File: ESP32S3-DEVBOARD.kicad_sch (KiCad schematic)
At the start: 61 parts, among them J1 PinHeader_1x22_P2.54mm_Vertic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, J2 PinHeader_1x22_P2.54mm_Vertic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, J3 G-Switch_GT-USB-7010ASV, J4 G-Switch_GT-USB-7010ASV, Q1 BC817-40,215, Q2 BC817-40,215, SW1 TS-1088-AR02016, SW2 TS-1088-AR02016, SW3 TS-1088-AR02016, SW4 TS-1088-AR02016, U1 AMS1117-3.3, U2 ESP32-S3-WROOM-1, U3 USBLC6-2P6, U4 CP2102N-A02-GQFN28R, U5 BMI270, U6 USBLC6-2P6

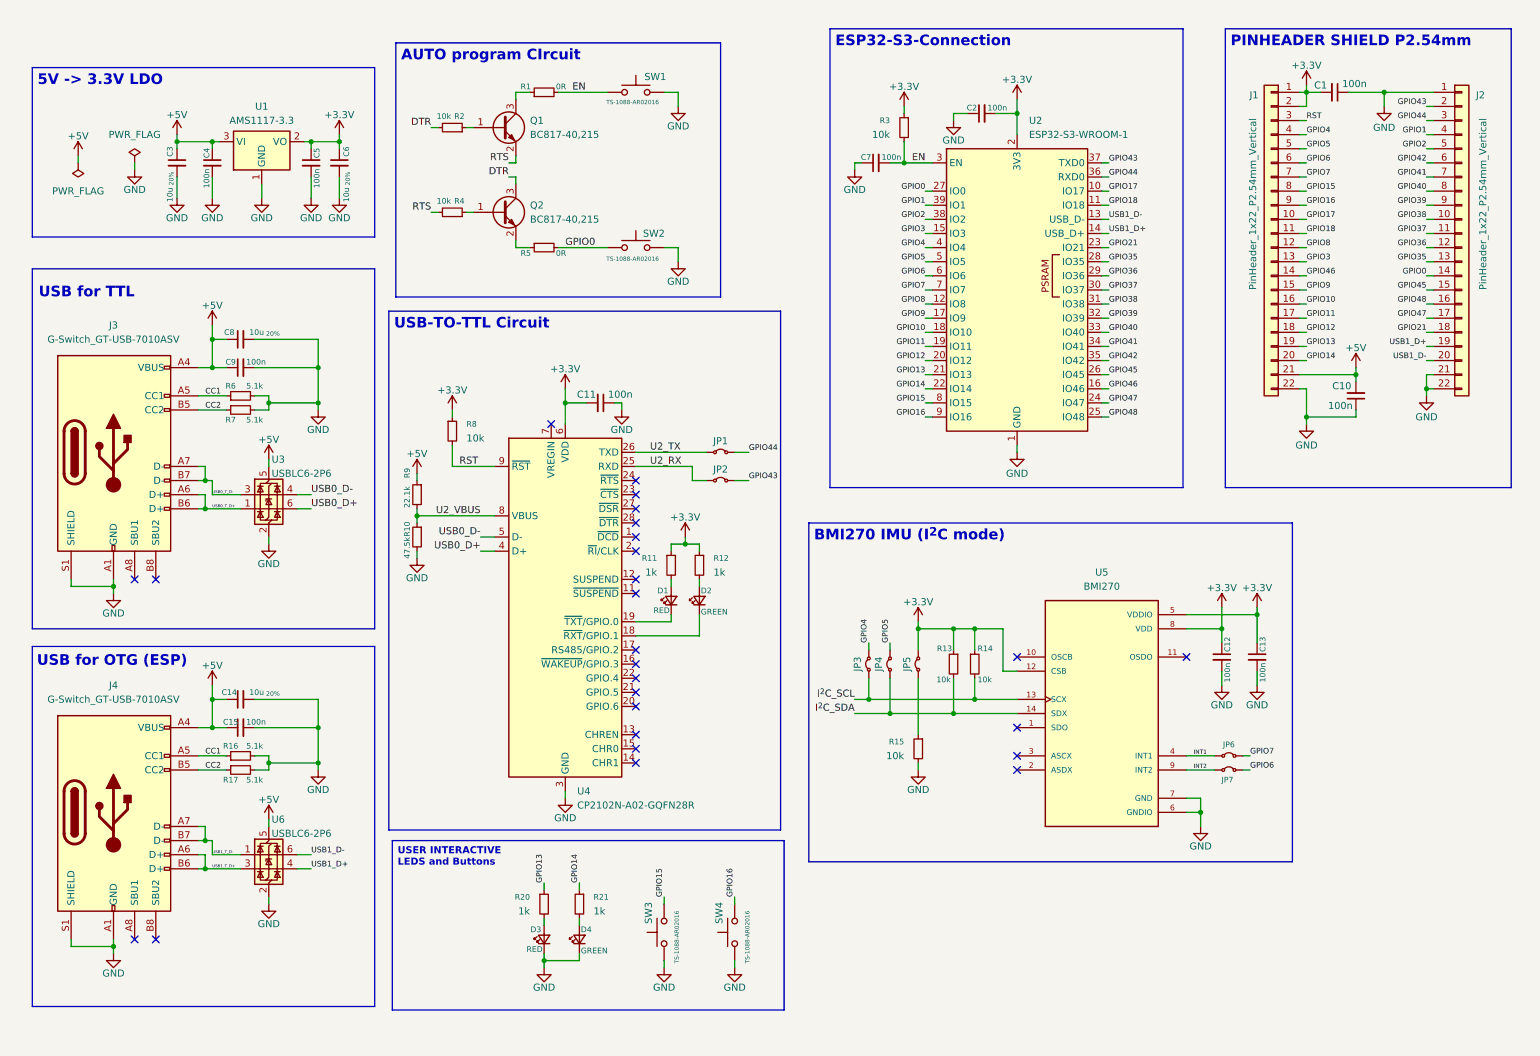
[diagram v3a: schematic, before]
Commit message: Removed jumpers, and added dipswitch to schematics
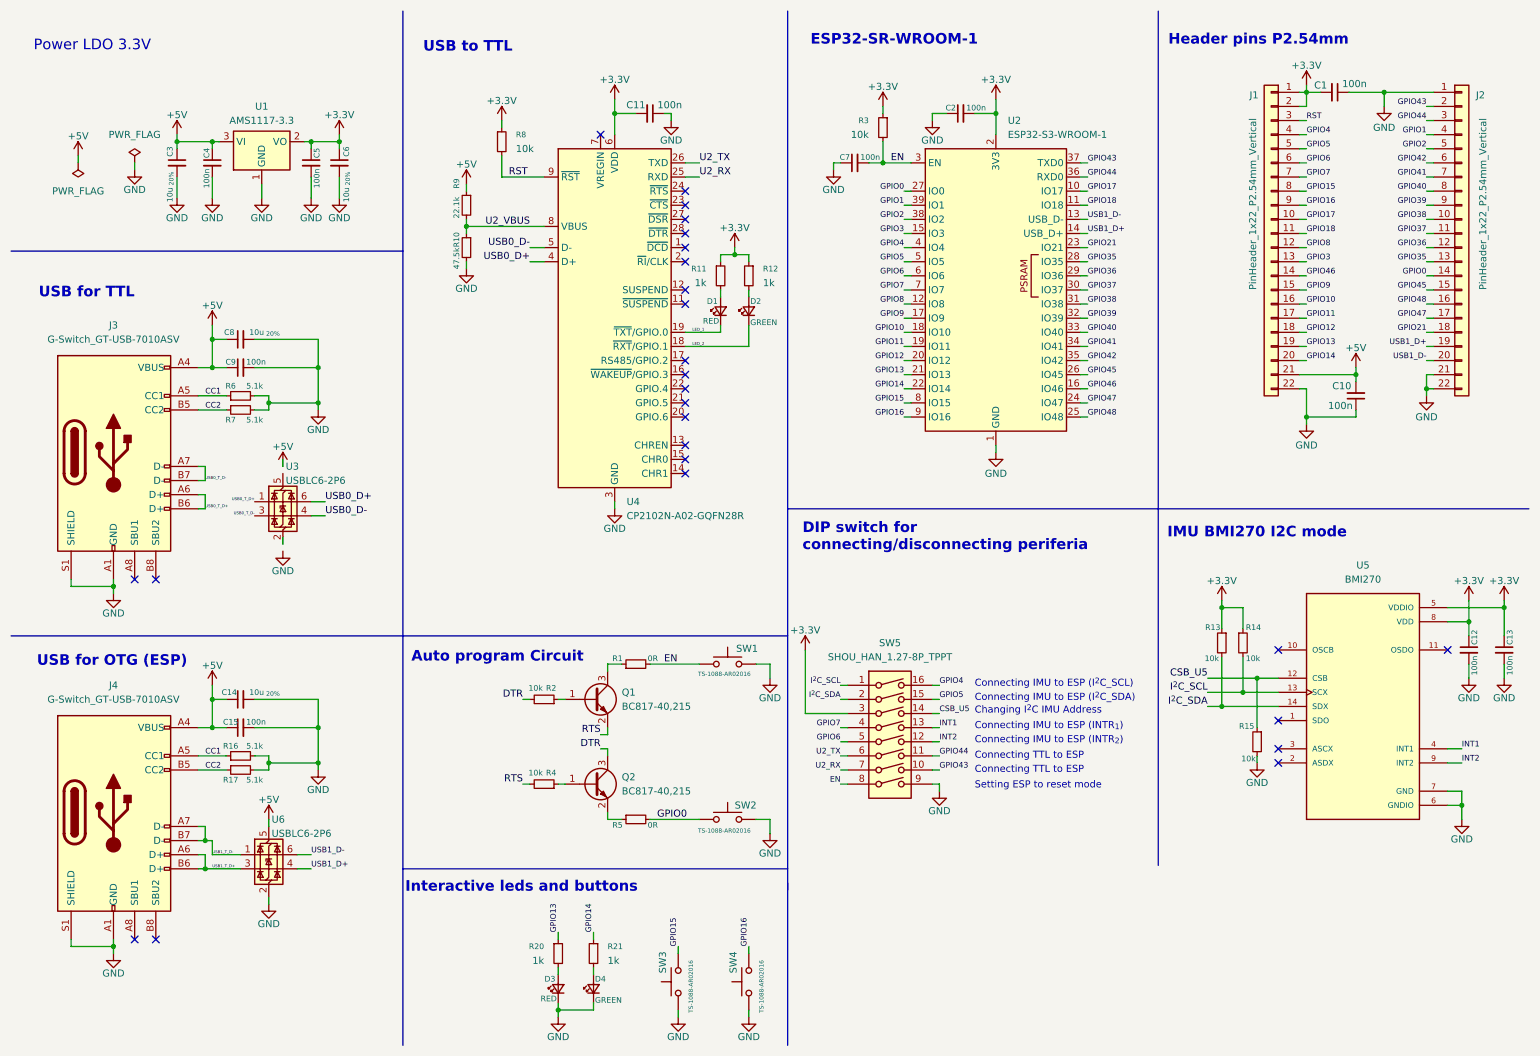
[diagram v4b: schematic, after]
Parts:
- removed JP1, JP2, JP3, JP4, JP5, JP6, JP7: Jumper_1x2_P2.54_Bridged, ESP32S3-DEVBOARD:Jumper_1x02_P2.54mm_Bridged, symbol ESP32S3-DEVBOARD:Jumper_1x2_P2.54_Bridged
- added SW5: SHOU_HAN_1.27-8P_TPPT, ESP32S3-DEVBOARD:SHOU_HAN_1.27-8P_TTPT, symbol ESP32S3-DEVBOARD:SHOU_HAN_1.27-8P_TPPT
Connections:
- net +3.3V: now also SW5.3; no longer U5.12 (CSB)
- net +5V: no longer U3.5 (VBUS)
- net EN: now also SW5.8
- net GND: now also SW5.9; no longer U3.2 (GND)
- net GPIO4: now also SW5.16
- net GPIO43: now also SW5.10
- net GPIO44: now also SW5.11
- net GPIO5: now also SW5.15
- net GPIO6: now also SW5.5
- net GPIO7: now also SW5.4
- net INT1: now also SW5.13
- net INT2: now also SW5.12
- net I^{2}C_SCL: now also SW5.1
- net I^{2}C_SDA: now also SW5.2
- net U2_RX: now also SW5.7
- net U2_TX: now also SW5.6
- net LED_2: now reaches D2.1 (K), U4.18 (~{RXT}/GPIO.1)
- net LED_1: now reaches D1.1 (K), U4.19 (~{TXT}/GPIO.0)
- net CSB_U5: now reaches R15.1
- net CSB_U5: now also U5.12 (CSB), SW5.14
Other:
- note added: "Auto program Circuit"
- note added: "Changing I^{2}C IMU Address"
- note added: "Connecting IMU to ESP (INTR_{1})"
- note added: "Connecting IMU to ESP (INTR_{2})"
- note added: "Connecting IMU to ESP (I^{2}C_SCL)"
- note added: "Connecting IMU to ESP (I^{2}C_SDA)"
- note added: "Connecting TTL to ESP"
- note added: "DIP switch for connecting/disconnecting periferia"
- note added: "ESP32-SR-WROOM-1"
- note added: "Header pins P2.54mm"
- note added: "IMU BMI270 I2C mode"
- note added: "Interactive leds and buttons"
- note added: "Power LDO 3.3V"
- note added: "Setting ESP to reset mode"
- note added: "USB to TTL"
- moved on the sheet: C11, C12, C13, C2, C7, D1, D2, D3, D4, Q1, Q2, R1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

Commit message: Changet position of ttl
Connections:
- net +3.3V: now also SW5.13; no longer SW5.3
- net +5V: now also U3.5 (VBUS)
- net CSB_U5: now also SW5.4; no longer SW5.14
- net EN: now also SW5.1; no longer SW5.8
- net GND: now also SW5.16, U3.2 (GND); no longer SW5.9
- net GPIO4: now also SW5.14; no longer SW5.16
- net GPIO43: now also SW5.9; no longer SW5.10
- net GPIO44: now also SW5.10; no longer SW5.11
- net GPIO6: now also SW5.11; no longer SW5.5
- net GPIO7: now also SW5.12; no longer SW5.4
- net INT1: now also SW5.5; no longer SW5.13
- net INT2: now also SW5.6; no longer SW5.12
- net I^{2}C_SCL: now also SW5.3; no longer SW5.1
- net U2_RX: now also SW5.8; no longer SW5.7
- net U2_TX: now also SW5.7; no longer SW5.6
- net CC1 renamed USB_0_CC1
- net USB_0_CC1: no longer J4.A5 (CC1), R16.1
- net CC2 renamed USB_0_CC2
- net USB_0_CC2: no longer J4.B5 (CC2), R17.1
- new net USB_1_CC1: J4.A5 (CC1), R16.1
- new net USB_1_CC2: J4.B5 (CC2), R17.1
- no-connect marks 26 -> 27
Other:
- moved on the sheet: R16, R17, R6, R7, SW5

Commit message: finish componemt placement
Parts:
- added C16: 100n, ESP32S3-DEVBOARD:C_0402_1005Metric, symbol ESP32S3-DEVBOARD:CL05B104KO5NNNC
- C10: now not fitted; now left out of the parts list
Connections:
- net +3.3V: now also SW5.11, C16.1; no longer SW5.13
- net CSB_U5: now also SW5.6; no longer SW5.4
- net DTR: now also U4.28 (~{DTR})
- net EN: now also J1.3 (Pin_3)
- net GND: now also C16.2
- net GPIO6: now also SW5.12; no longer SW5.11
- net GPIO7: now also SW5.13; no longer SW5.12
- net INT1: now also SW5.4; no longer SW5.5
- net INT2: now also SW5.5; no longer SW5.6
- net RST: no longer J1.3 (Pin_3)
- net RTS: now also U4.24 (~{RTS})
- no-connect marks 27 -> 25
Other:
- moved on the sheet: C11, C3, C4, C5, C6, R10, R8, R9, U1, U4

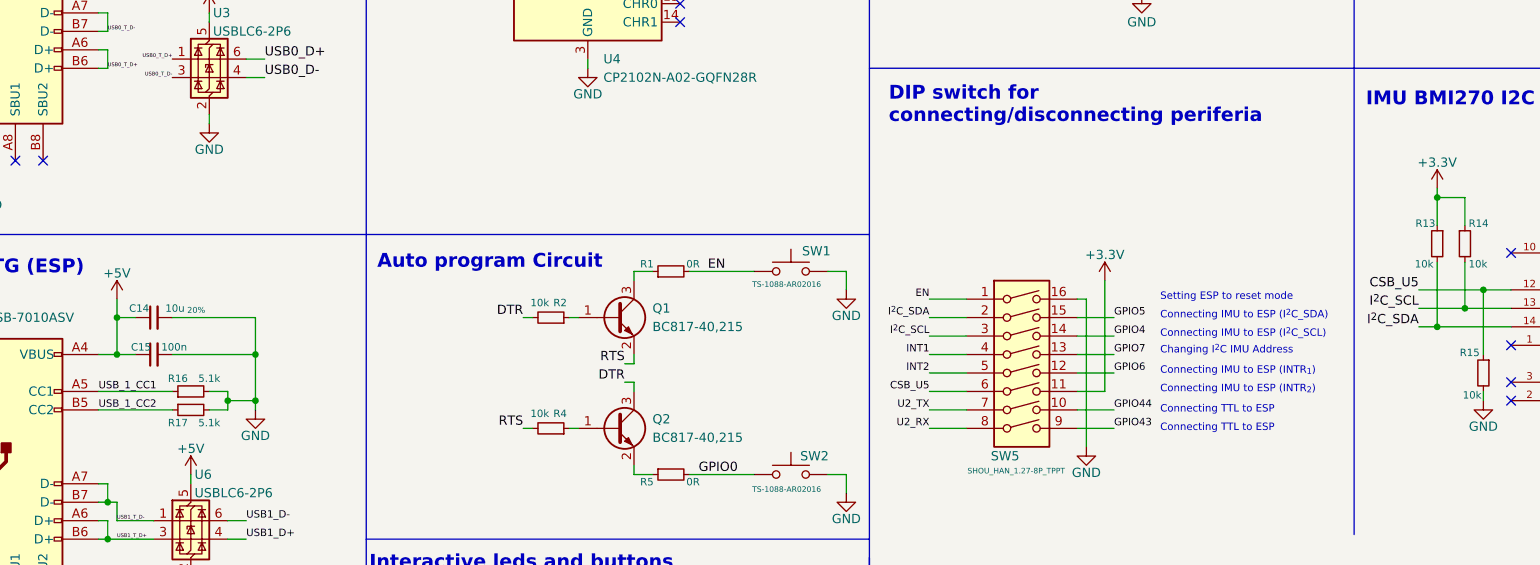
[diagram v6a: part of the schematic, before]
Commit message: fixed all errors (edit footprint silkskreens)
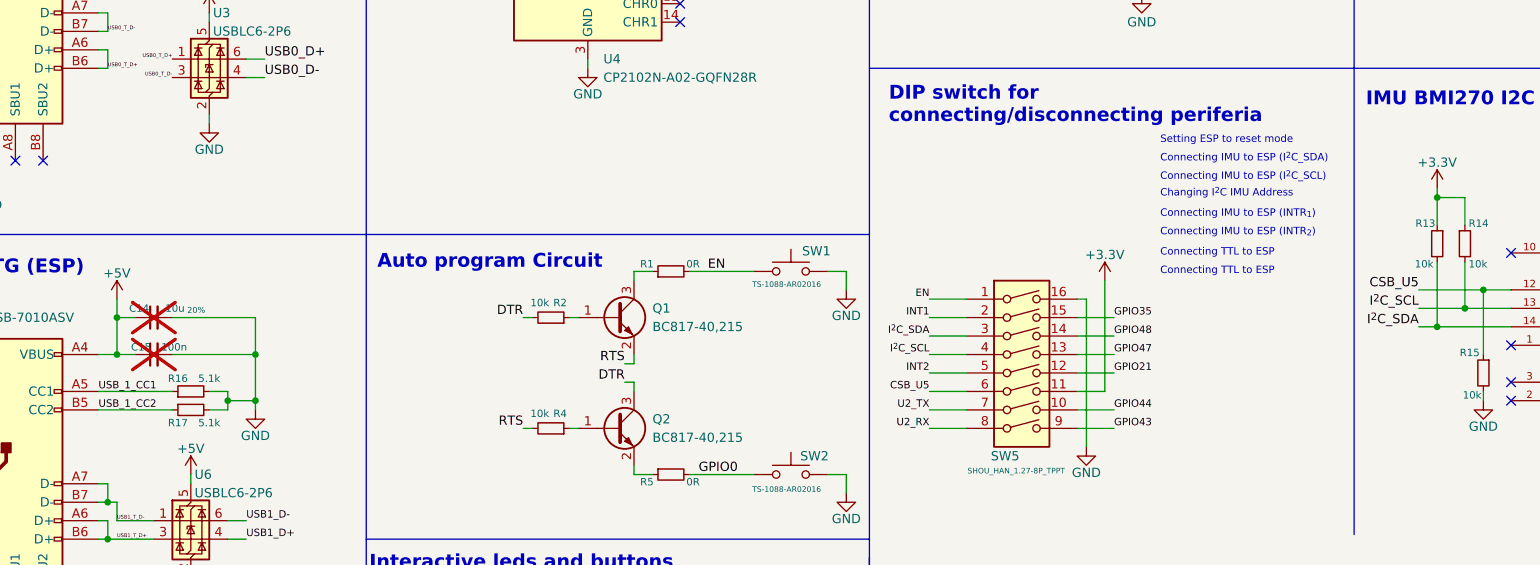
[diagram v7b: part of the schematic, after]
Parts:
- C14, C15: now not fitted; now left out of the parts list
- J1, J2: footprint ESP32S3-DEVBOARD:PinHeader_1x22_P2.54mm_Vertical -> ESP32S3-DEVBOARD:PinHeader_1x22_P2.54mm_Vertical_FLIPPED
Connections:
- net GPIO21: now also SW5.12
- net GPIO35: now also SW5.15
- net GPIO4: no longer SW5.14
- net GPIO47: now also SW5.13
- net GPIO48: now also SW5.14
- net GPIO5: no longer SW5.15
- net GPIO6: no longer SW5.12
- net GPIO7: no longer SW5.13
- net INT1: now also SW5.2; no longer SW5.4
- net I^{2}C_SCL: now also SW5.4; no longer SW5.3
- net I^{2}C_SDA: now also SW5.3; no longer SW5.2
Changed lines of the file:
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@@
 	(text "Connecting TTL to ESP"
 		(exclude_from_sim no)
-		(at 191.77 151.13 0)
+		(at 191.77 129.54 0)
 		(effects
 			(font
@@
 	(text "Connecting IMU to ESP (INTR_{2})"
 		(exclude_from_sim no)
-		(at 191.77 145.796 0)
+		(at 191.77 124.206 0)
 		(effects
 			(font
@@
 	(text "Changing I^{2}C IMU Address"
 		(exclude_from_sim no)
-		(at 191.77 140.462 0)
+		(at 191.77 118.872 0)
 		(effects
 			(font
@@
 	(text "Connecting IMU to ESP (I^{2}C_SCL)\n"
 		(exclude_from_sim no)
-		(at 191.77 138.176 0)
+		(at 191.77 116.586 0)
 		(effects
 			(font
@@
 	(text "Connecting TTL to ESP"
 		(exclude_from_sim no)
-		(at 191.77 148.59 0)
+		(at 191.77 127 0)
 		(effects
 			(font
@@
 	(text "Connecting IMU to ESP (INTR_{1})"
 		(exclude_from_sim no)
-		(at 191.77 143.256 0)
+		(at 191.77 121.666 0)
 		(effects
 			(font
@@
 	(text "Setting ESP to reset mode"
 		(exclude_from_sim no)
-		(at 191.77 133.096 0)
+		(at 191.77 111.506 0)
 		(effects
 			(font
@@
 	(text "Connecting IMU to ESP (I^{2}C_SDA)\n"
 		(exclude_from_sim no)
-		(at 191.77 135.636 0)
+		(at 191.77 114.046 0)
 		(effects
 			(font
@@
 	(wire
 		(pts
-			(xy 160.02 138.43) (xy 165.1 138.43)
+			(xy 160.02 140.97) (xy 165.1 140.97)
 		)
 		(stroke
@@
 	(wire
 		(pts
-			(xy 160.02 140.97) (xy 165.1 140.97)
+			(xy 160.02 135.89) (xy 165.1 135.89)
 		)
 		(stroke
@@
 	(wire
 		(pts
-			(xy 185.42 135.89) (xy 180.34 135.89)
+			(xy 185.42 138.43) (xy 180.34 138.43)
 		)
 		(stroke
@@
 	(wire
 		(pts
-			(xy 185.42 140.97) (xy 180.34 140.97)
+			(xy 185.42 135.89) (xy 180.34 135.89)
 		)
 		(stroke
@@
 	(wire
 		(pts
-			(xy 160.02 135.89) (xy 165.1 135.89)
+			(xy 160.02 138.43) (xy 165.1 138.43)
 		)
 		(stroke
@@
 	(wire
 		(pts
-			(xy 185.42 138.43) (xy 180.34 138.43)
+			(xy 185.42 140.97) (xy 180.34 140.97)
 		)
 		(stroke
@@
 	)
 	(label "I^{2}C_SDA"
-		(at 160.02 135.89 180)
+		(at 160.02 138.43 180)
 		(effects
 			(font
@@
 	)
 	(label "I^{2}C_SCL"
-		(at 160.02 138.43 180)
+		(at 160.02 140.97 180)
 		(effects
 			(font
@@
 		)
 	)
-	(label "GPIO6"
+	(label "GPIO21"
 		(at 185.42 143.51 0)
 		(effects
@@
 		)
 	)
-	(label "GPIO5"
-		(at 185.42 135.89 0)
+	(label "GPIO48"
+		(at 185.42 138.43 0)
 		(effects
 			(font
@@
 		)
 	)
-	(label "GPIO7"
-		(at 185.42 140.97 0)
+	(label "GPIO35"
+		(at 185.42 135.89 0)
 		(effects
 			(font
@@
 		)
 	)
-	(label "GPIO4"
-		(at 185.42 138.43 0)
+	(label "GPIO47"
+		(at 185.42 140.97 0)
 		(effects
 			(font
@@
 	)
 	(label "INT1"
-		(at 160.02 140.97 180)
+		(at 160.02 135.89 180)
 		(effects
 			(font
@@
 		(unit 1)
 		(exclude_from_sim no)
-		(in_bom yes)
-		(on_board yes)
-		(dnp no)
+		(in_bom no)
+		(on_board no)
+		(dnp yes)
 		(property "Reference" "C15"
 			(at 51.562 139.954 90)
@@
 			)
 		)
-		(property "Footprint" "ESP32S3-DEVBOARD:PinHeader_1x22_P2.54mm_Vertical"
+		(property "Footprint" "ESP32S3-DEVBOARD:PinHeader_1x22_P2.54mm_Vertical_FLIPPED"
 			(at 273.05 52.07 0)
 			(effects
@@
 			)
 		)
-		(property "Footprint" "ESP32S3-DEVBOARD:PinHeader_1x22_P2.54mm_Vertical"
+		(property "Footprint" "ESP32S3-DEVBOARD:PinHeader_1x22_P2.54mm_Vertical_FLIPPED"
 			(at 238.76 52.07 0)
 			(effects
@@
 		(unit 1)
 		(exclude_from_sim no)
-		(in_bom yes)
-		(on_board yes)
-		(dnp no)
+		(in_bom no)
+		(on_board no)
+		(dnp yes)
 		(property "Reference" "C14"
 			(at 51.308 134.62 90)

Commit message: Finnished the board!! :)
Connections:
- net LED_1 renamed TX_LED
- net LED_2 renamed RX_LED
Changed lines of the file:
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@@
 		)
 	)
-	(label "LED_1"
+	(label "TX_LED"
 		(at 127 69.85 0)
 		(effects
@@
 		)
 	)
-	(label "LED_2"
+	(label "RX_LED"
 		(at 127 72.39 0)
 		(effects
